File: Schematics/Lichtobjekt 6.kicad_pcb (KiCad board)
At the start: 2 copper layers, 99.8 x 35 mm, 129 parts, among them IC1 STM32F10XCXT6, IC2 TSOP348, IC3 MCP1703DB 3.0V, IC4 RV-3029-C2, IC6 24SN, J1 22-27-2031-03, J2 22-?-0227-2021, J3 22-?-0227-2021, J4 22-?-0227-2021, J5 22-?-0227-2021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

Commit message: version of PCB produced first version to show basic functionality incl. remote and serial monitor output
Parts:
- removed REF** (x4): MountingHole_3.2mm_M3_DIN965_Pad, MountingHole:MountingHole_3.2mm_M3_DIN965_Pad
- R17, R31, R33: value 10k -> 10k 0.1%
- R2, R32: value 100k -> 33k 0.1%
- R30: value 33k -> 33k 0.1%
- moved C7 8.89 mm to (133.3, 120.7), turned to 0 degrees
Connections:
- IC1 pad 1: VBACKUP -> +UB3
- T3 pad 2: Net-(LED1-PadK) -> GND
- T3 pad 3: GND -> Net-(LED1-PadK)
- T4 pad 2: Net-(R11-Pad2) -> GND
- T4 pad 3: GND -> Net-(R11-Pad2)
- T5 pad 2: Net-(R13-Pad2) -> GND
- T5 pad 3: GND -> Net-(R13-Pad2)
- T6 pad 2: Net-(R12-Pad2) -> GND
- T6 pad 3: GND -> Net-(R12-Pad2)
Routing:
- net VBACKUP: track 52.1 -> 41.6 mm
- net +UB3: track 229.9 -> 231.9 mm

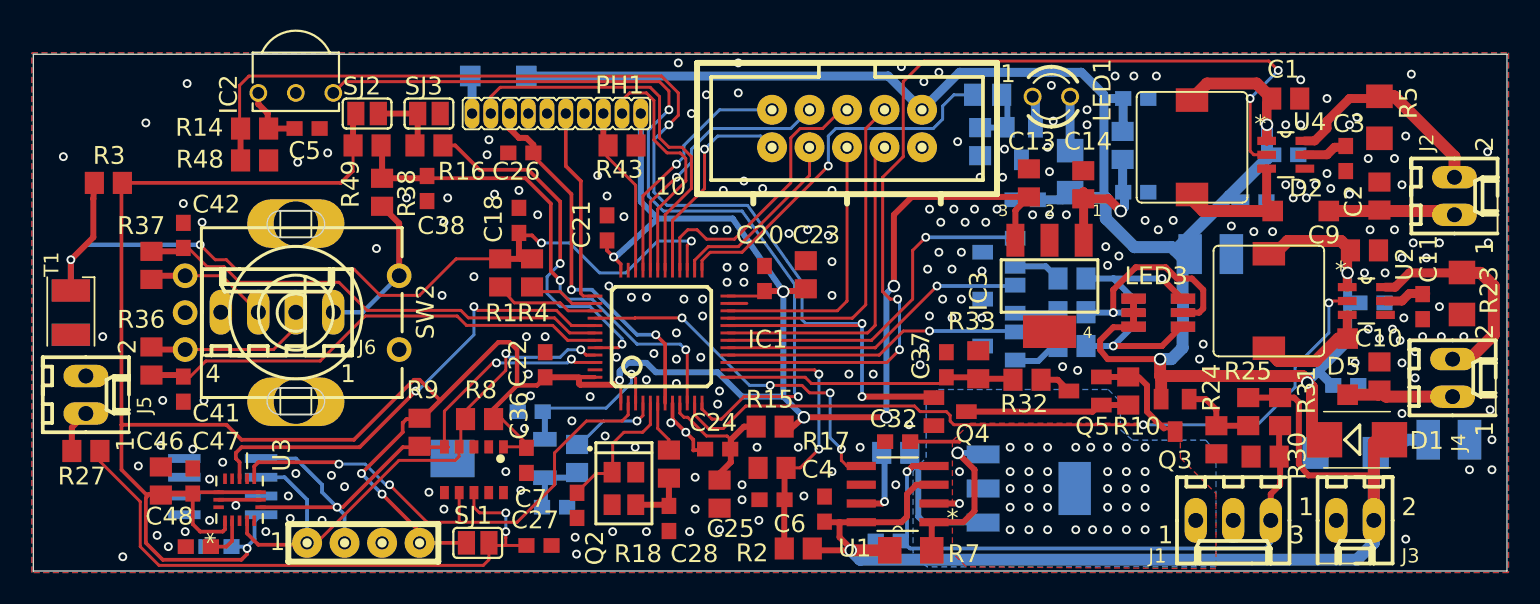
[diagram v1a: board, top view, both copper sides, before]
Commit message: added battery deep power down added measures to minimize power consumption in stop mode
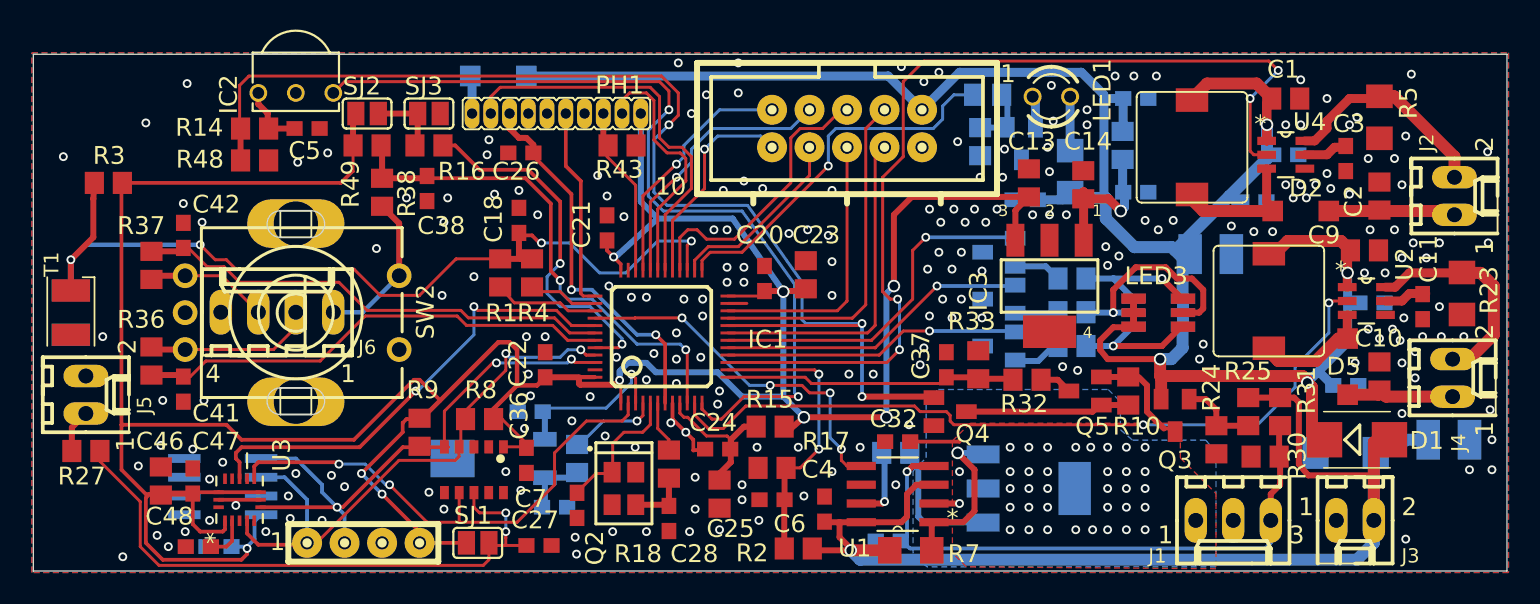
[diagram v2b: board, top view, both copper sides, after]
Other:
- net class Default removed
